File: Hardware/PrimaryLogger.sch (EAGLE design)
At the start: 91 parts, among them J1 CONN_42.54_SCREW, J2 CONN_42.54_SCREW, J3 CONN_42.54_SCREW, J4 CONN_42.54_SCREW, J5 CONN_32.54_SCREW, J9 GEMS_POWER_PLUGINPUT, Q1 DMG3404, Q2 DMG3404, U1 MCP79412SOIC, U10 PCA9617TSSOP8, U11 SN74AUP3G34DCU, U12 SN74LVC1G3157SC70, U2 TPL5010DDC, U3 MCP23008SSOP, U4 SHTC3DFN, U5 TCS3400, U6 TPL5010DDC, U7 MIC2005, U8 MIC2005, U9 MIC842L

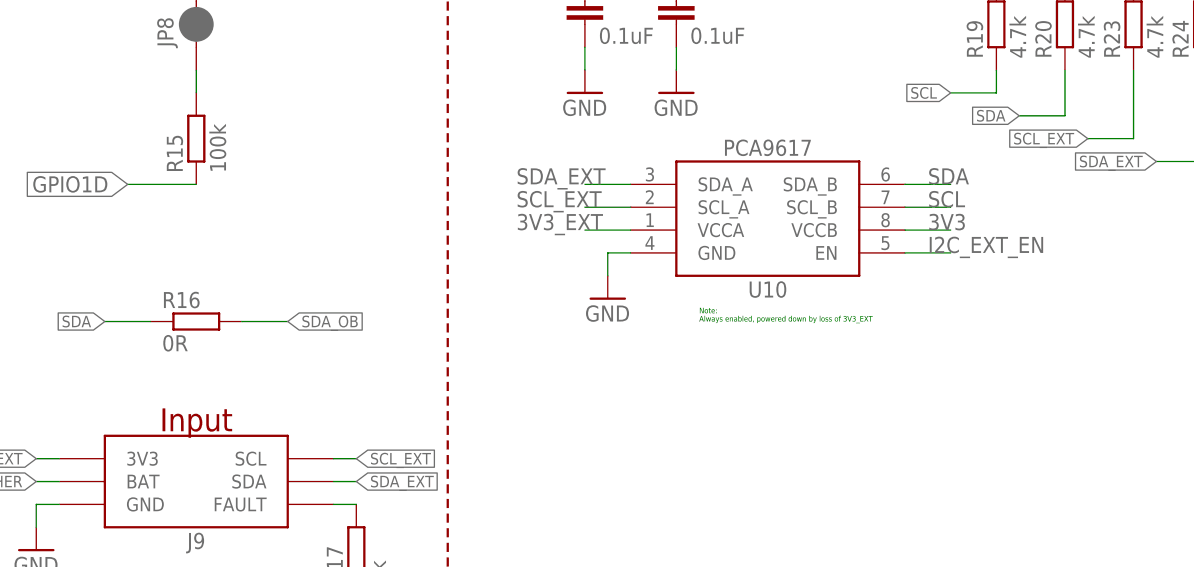
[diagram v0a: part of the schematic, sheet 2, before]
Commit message: Minor updates v0.4A sent to fab
Fixed layout issues and changed power topology for I2C buffer
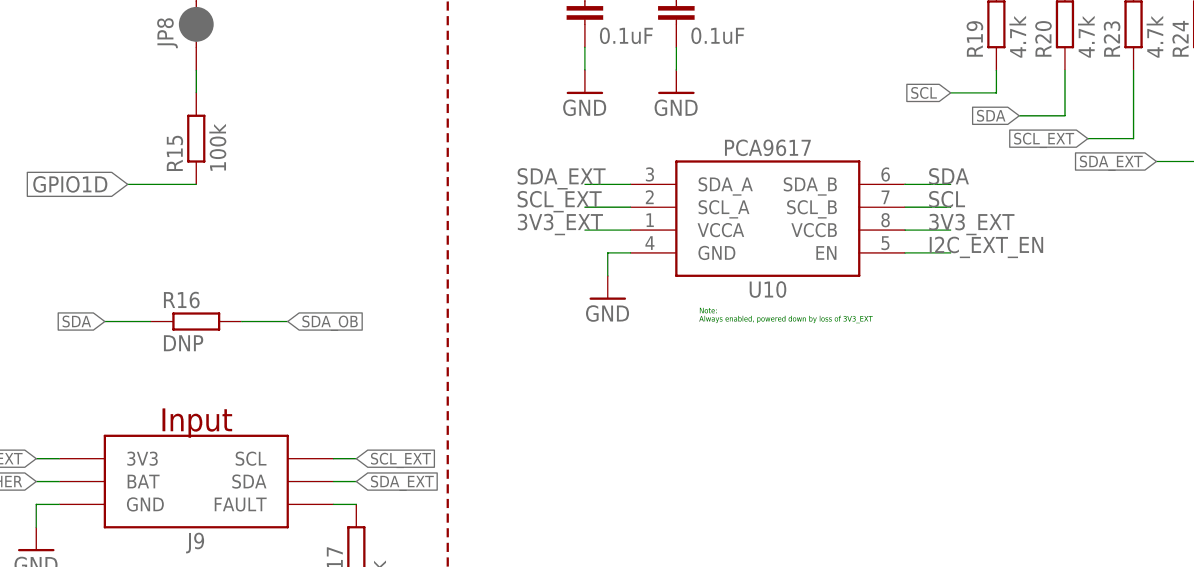
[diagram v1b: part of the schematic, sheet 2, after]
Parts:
- R16: value 0R -> DNP
- U10: value PCA9617TSSOP8 -> PCA9617; device bschulz:PCA9617TSSOP8 -> bschulz:PCA9617
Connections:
- net 3V3: no longer U10.VCCB
- net 3V3_EXT: now also U10.VCCB
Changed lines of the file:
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@@
 <attribute name="DESIGNER" value="Bobby Schulz"/>
 <attribute name="PROJECT" value="Hyena"/>
-<attribute name="REV" value="0.2"/>
+<attribute name="REV" value="0.4"/>
 </part>
 <part name="FRAME2" library="bschulz" deviceset="FRAME_A_L" device="">
 <attribute name="DESIGNER" value="Bobby Schulz"/>
 <attribute name="PROJECT" value="Hyena"/>
-<attribute name="REV" value="0.2"/>
+<attribute name="REV" value="0.4"/>
 </part>
 <part name="C1" library="bschulz_passives" deviceset="C-EU" device="C0603" technology="0.1UF" value="0.1uF"/>
@@
 <part name="GND31" library="supply1" library_urn="urn:adsk.eagle:library:371" deviceset="GND" device=""/>
 <part name="GND32" library="supply1" library_urn="urn:adsk.eagle:library:371" deviceset="GND" device=""/>
-<part name="U10" library="bschulz" deviceset="PCA9617" device="TSSOP8"/>
+<part name="U10" library="bschulz" deviceset="PCA9617" device=""/>
 <part name="GND33" library="supply1" library_urn="urn:adsk.eagle:library:371" deviceset="GND" device=""/>
 <part name="C16" library="bschulz_passives" deviceset="C-EU" device="C0603" technology="0.1UF" value="0.1uF"/>
@@
 <part name="GND38" library="supply1" library_urn="urn:adsk.eagle:library:371" deviceset="GND" device=""/>
 <part name="R2" library="bschulz_passives" deviceset="R-EU_" device="R0603" technology="0.0" value="0R"/>
-<part name="R16" library="bschulz_passives" deviceset="R-EU_" device="R0603" technology="0.0" value="0R"/>
+<part name="R16" library="bschulz_passives" deviceset="R-EU_" device="R0603" technology="0.0" value="DNP"/>
 </parts>
 <sheets>
@@
 </segment>
 <segment>
-<pinref part="U10" gate="G$1" pin="VCCB"/>
-<wire x1="223.52" y1="76.2" x2="228.6" y2="76.2" width="0.1524" layer="91"/>
-<label x="226.06" y="76.2" size="1.778" layer="95"/>
-</segment>
-<segment>
 <pinref part="C16" gate="G$1" pin="1"/>
 <wire x1="187.96" y1="104.14" x2="187.96" y2="106.68" width="0.1524" layer="91"/>
@@
 <label x="127" y="50.8" size="1.27" layer="95" rot="R180" xref="yes"/>
 </segment>
-</net>
+<segment>
+<pinref part="U10" gate="G$1" pin="VCCB"/>
+<wire x1="223.52" y1="76.2" x2="228.6" y2="76.2" width="0.1524" layer="91"/>
+<label x="226.06" y="76.2" size="1.778" layer="95"/>
+</segment>
+</net>

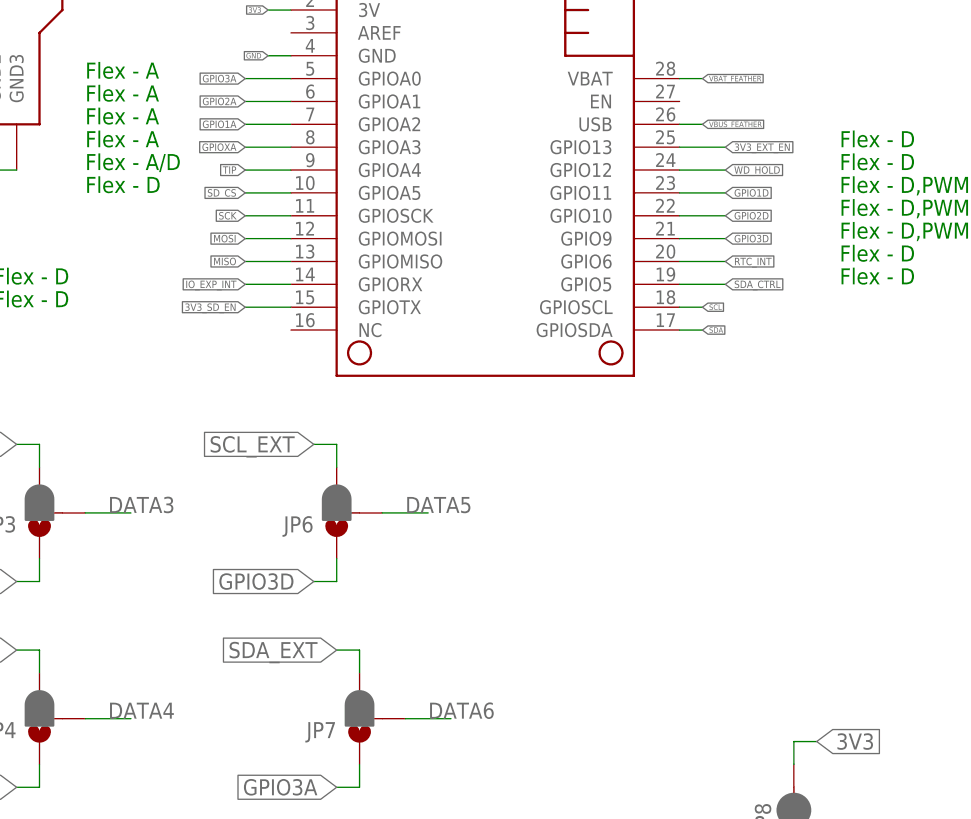
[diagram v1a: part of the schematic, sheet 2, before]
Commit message: v1.0 Updates
Changed pinout and added connector to support preliminary talon development
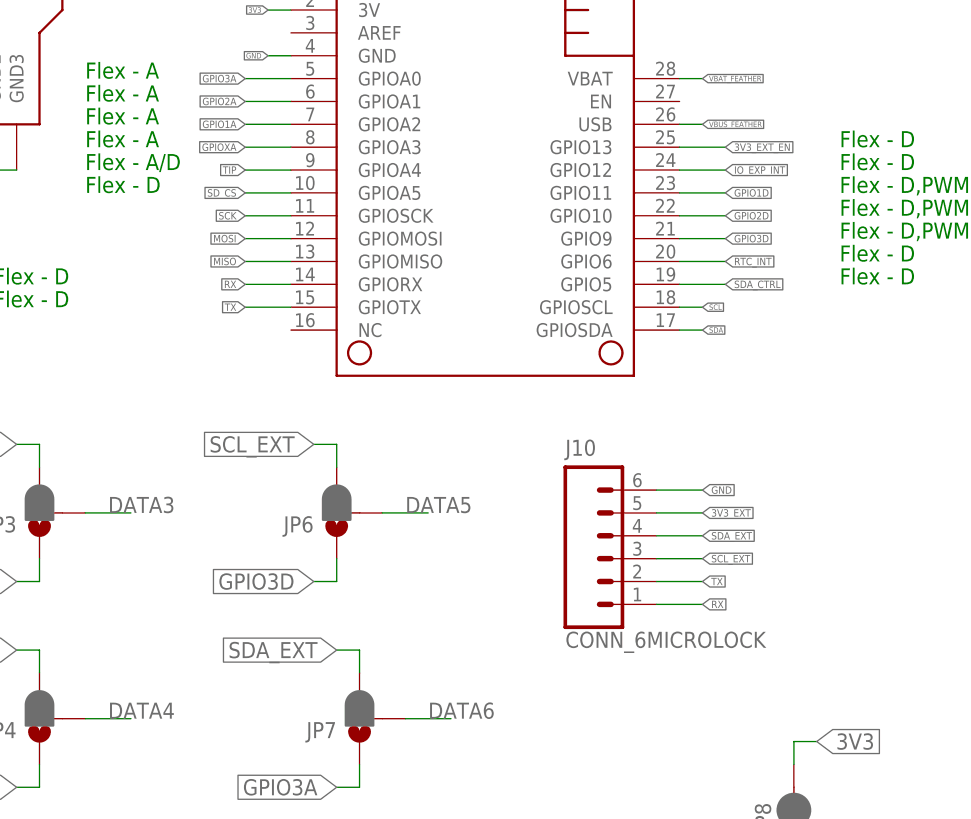
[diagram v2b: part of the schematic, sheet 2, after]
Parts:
- added J10: CONN_6MICROLOCK, bschulz:CONN_6MICROLOCK
- MS1: value FEATHERWING_NODIM -> FEATHERWINGLAYOUT; device bschulz:FEATHERWING_NODIM -> bschulz:FEATHERWINGLAYOUT
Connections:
- new net RX: J10.1, MS1.GPIORX
- new net TX: J10.2, MS1.GPIOTX
- net 3V3_EXT: now also J10.5
- net 3V3_SD_EN: now also U3.GP7; no longer MS1.GPIOTX
- net GND: now also J10.6
- net IO_EXP_INT: now also MS1.GPIO12; no longer MS1.GPIORX
- net SCL_EXT: now also J10.3
- net SDA_EXT: now also J10.4
- net WD_HOLD: now also U3.GP6; no longer MS1.GPIO12
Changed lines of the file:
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@@
 <part name="GND43" library="supply1" library_urn="urn:adsk.eagle:library:371" deviceset="GND" device=""/>
 <part name="U11" library="bschulz" deviceset="SN74AUP3G34" device="DCU"/>
-<part name="MS1" library="bschulz" deviceset="FEATHERWING" device="_NODIM"/>
+<part name="MS1" library="bschulz" deviceset="FEATHERWING" device="LAYOUT" value="FEATHERWINGLAYOUT"/>
 <part name="U8" library="bschulz" deviceset="MIC2005" device=""/>
 <part name="C12" library="bschulz_passives" deviceset="C-EU" device="C0603" technology="1UF" value="1uF"/>
@@
 <attribute name="DESIGNER" value="Bobby Schulz"/>
 <attribute name="PROJECT" value="Hyena"/>
-<attribute name="REV" value="0.4"/>
+<attribute name="REV" value="v1.0"/>
 </part>
 <part name="FRAME2" library="bschulz" deviceset="FRAME_A_L" device="">
 <attribute name="DESIGNER" value="Bobby Schulz"/>
 <attribute name="PROJECT" value="Hyena"/>
-<attribute name="REV" value="0.4"/>
+<attribute name="REV" value="v1.0"/>
 </part>
 <part name="C1" library="bschulz_passives" deviceset="C-EU" device="C0603" technology="0.1UF" value="0.1uF"/>
@@
 <part name="R2" library="bschulz_passives" deviceset="R-EU_" device="R0603" technology="0.0" value="0R"/>
 <part name="R16" library="bschulz_passives" deviceset="R-EU_" device="R0603" technology="0.0" value="DNP"/>
+<part name="J10" library="bschulz" deviceset="CONN_6" device="MICROLOCK"/>
 </parts>
 <sheets>
@@
 <label x="73.66" y="129.54" size="1.778" layer="95"/>
 </segment>
+<segment>
+<pinref part="U3" gate="G$1" pin="GP6"/>
+<wire x1="76.2" y1="190.5" x2="83.82" y2="190.5" width="0.1524" layer="91"/>
+<label x="78.74" y="190.5" size="1.778" layer="95"/>
+</segment>
 </net>
 <net name="N$3" class="0">
@@
 <wire x1="53.34" y1="76.2" x2="50.8" y2="76.2" width="0.1524" layer="91"/>
 <label x="50.8" y="76.2" size="1.778" layer="95" rot="R180" xref="yes"/>
+</segment>
+<segment>
+<pinref part="U3" gate="G$1" pin="GP7"/>
+<wire x1="76.2" y1="193.04" x2="83.82" y2="193.04" width="0.1524" layer="91"/>
+<label x="78.74" y="193.04" size="1.778" layer="95"/>
 </segment>
 </net>
@@
 <attribute name="VALUE" x="140.97" y="62.738" size="1.778" layer="96"/>
 </instance>
+<instance part="J10" gate="G$1" x="119.38" y="119.38" smashed="yes">
+<attribute name="VALUE" x="119.38" y="117.094" size="1.778" layer="96" font="vector"/>
+<attribute name="NAME" x="119.38" y="138.43" size="1.778" layer="95" font="vector"/>
+</instance>
 </instances>
 <busses>
@@
 <pinref part="GND38" gate="1" pin="GND"/>
 </segment>
+<segment>
+<pinref part="J10" gate="G$1" pin="6"/>
+<wire x1="129.54" y1="134.62" x2="134.62" y2="134.62" width="0.1524" layer="91"/>
+<label x="134.62" y="134.62" size="0.8128" layer="95" xref="yes"/>
+</segment>
 </net>
 <net name="SDA" class="0">
@@
 <label x="226.06" y="76.2" size="1.778" layer="95"/>
 </segment>
+<segment>
+<pinref part="J10" gate="G$1" pin="5"/>
+<wire x1="129.54" y1="132.08" x2="134.62" y2="132.08" width="0.1524" layer="91"/>
+<label x="134.62" y="132.08" size="0.8128" layer="95" xref="yes"/>
+</segment>
 </net>
 <net name="SDA_EXT" class="0">
@@
 <label x="162.56" y="48.26" size="1.27" layer="95" xref="yes"/>
 </segment>
+<segment>
+<pinref part="J10" gate="G$1" pin="4"/>
+<wire x1="129.54" y1="129.54" x2="134.62" y2="129.54" width="0.1524" layer="91"/>
+<label x="134.62" y="129.54" size="0.8128" layer="95" xref="yes"/>
+</segment>
 </net>
 <net name="SCL_EXT" class="0">
@@
 <wire x1="160.02" y1="50.8" x2="162.56" y2="50.8" width="0.1524" layer="91"/>
 <label x="162.56" y="50.8" size="1.27" layer="95" xref="yes"/>
+</segment>
+<segment>
+<pinref part="J10" gate="G$1" pin="3"/>
+<wire x1="129.54" y1="127" x2="134.62" y2="127" width="0.1524" layer="91"/>
+<label x="134.62" y="127" size="0.8128" layer="95" xref="yes"/>
 </segment>
 </net>
@@
 </segment>
 </net>
-<net name="WD_HOLD" class="0">
-<segment>
-<pinref part="MS1" gate="G$1" pin="GPIO12"/>
-<wire x1="132.08" y1="170.18" x2="137.16" y2="170.18" width="0.1524" layer="91"/>
-<label x="137.16" y="170.18" size="0.8128" layer="95" xref="yes"/>
-</segment>
-</net>
 <net name="MISO" class="0">
 <segment>
@@
 </segment>
 </net>
-<net name="3V3_SD_EN" class="0">
-<segment>
-<pinref part="MS1" gate="G$1" pin="GPIOTX"/>
-<wire x1="88.9" y1="154.94" x2="83.82" y2="154.94" width="0.1524" layer="91"/>
-<label x="83.82" y="154.94" size="0.8128" layer="95" rot="R180" xref="yes"/>
-</segment>
-</net>
 <net name="SDA_CTRL" class="0">
 <segment>
@@
 <net name="IO_EXP_INT" class="0">
 <segment>
-<pinref part="MS1" gate="G$1" pin="GPIORX"/>
-<wire x1="88.9" y1="157.48" x2="83.82" y2="157.48" width="0.1524" layer="91"/>
-<label x="83.82" y="157.48" size="0.8128" layer="95" rot="R180" xref="yes"/>
+<pinref part="MS1" gate="G$1" pin="GPIO12"/>
+<wire x1="132.08" y1="170.18" x2="137.16" y2="170.18" width="0.1524" layer="91"/>
+<label x="137.16" y="170.18" size="0.8128" layer="95" xref="yes"/>
 </segment>
 </net>
@@
 </segment>
 </net>
+<net name="TX" class="0">
+<segment>
+<pinref part="MS1" gate="G$1" pin="GPIOTX"/>
+<wire x1="88.9" y1="154.94" x2="83.82" y2="154.94" width="0.1524" layer="91"/>
+<label x="83.82" y="154.94" size="0.8128" layer="95" rot="R180" xref="yes"/>
+</segment>
+<segment>
+<pinref part="J10" gate="G$1" pin="2"/>
+<wire x1="129.54" y1="124.46" x2="134.62" y2="124.46" width="0.1524" layer="91"/>
+<label x="134.62" y="124.46" size="0.8128" layer="95" xref="yes"/>
+</segment>
+</net>
+<net name="RX" class="0">
+<segment>
+<pinref part="MS1" gate="G$1" pin="GPIORX"/>
+<wire x1="88.9" y1="157.48" x2="83.82" y2="157.48" width="0.1524" layer="91"/>
+<label x="83.82" y="157.48" size="0.8128" layer="95" rot="R180" xref="yes"/>
+</segment>
+<segment>
+<pinref part="J10" gate="G$1" pin="1"/>
+<wire x1="129.54" y1="121.92" x2="134.62" y2="121.92" width="0.1524" layer="91"/>
+<label x="134.62" y="121.92" size="0.8128" layer="95" xref="yes"/>
+</segment>
+</net>
